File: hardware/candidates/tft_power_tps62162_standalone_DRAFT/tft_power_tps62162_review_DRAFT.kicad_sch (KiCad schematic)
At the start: 8 parts, among them U301 TPS62162DSGR

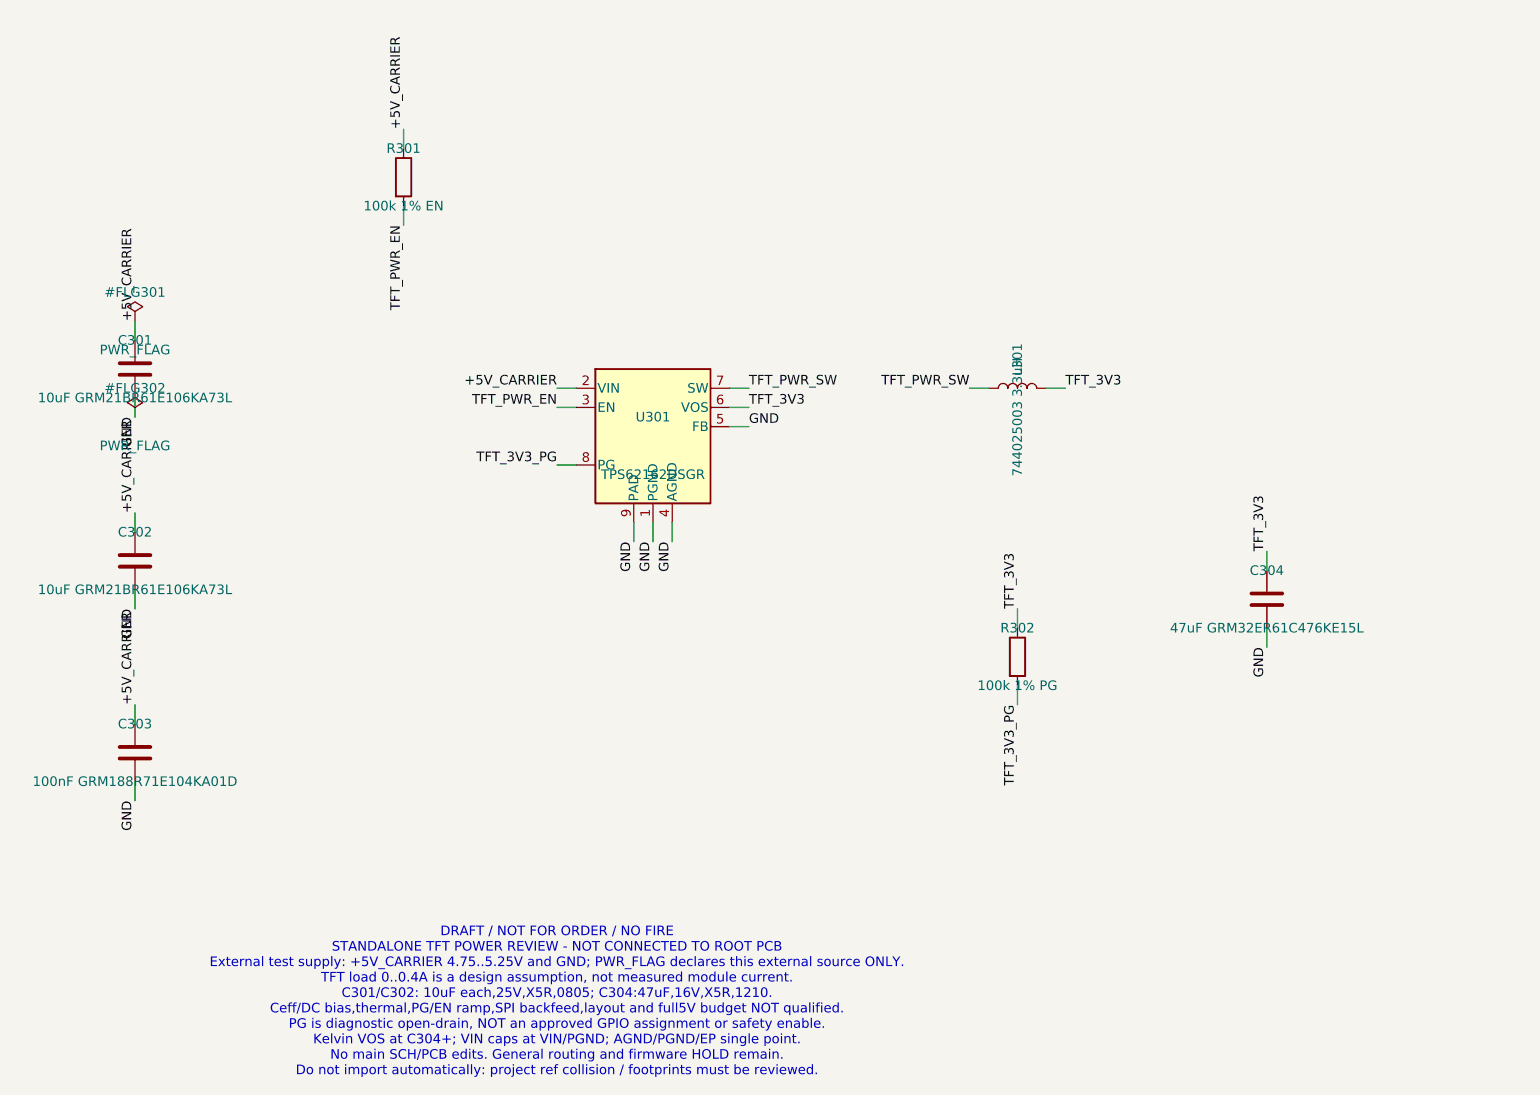
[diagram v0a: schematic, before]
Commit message: hardware: fix TPS62162 draft fields and identify pull-ups
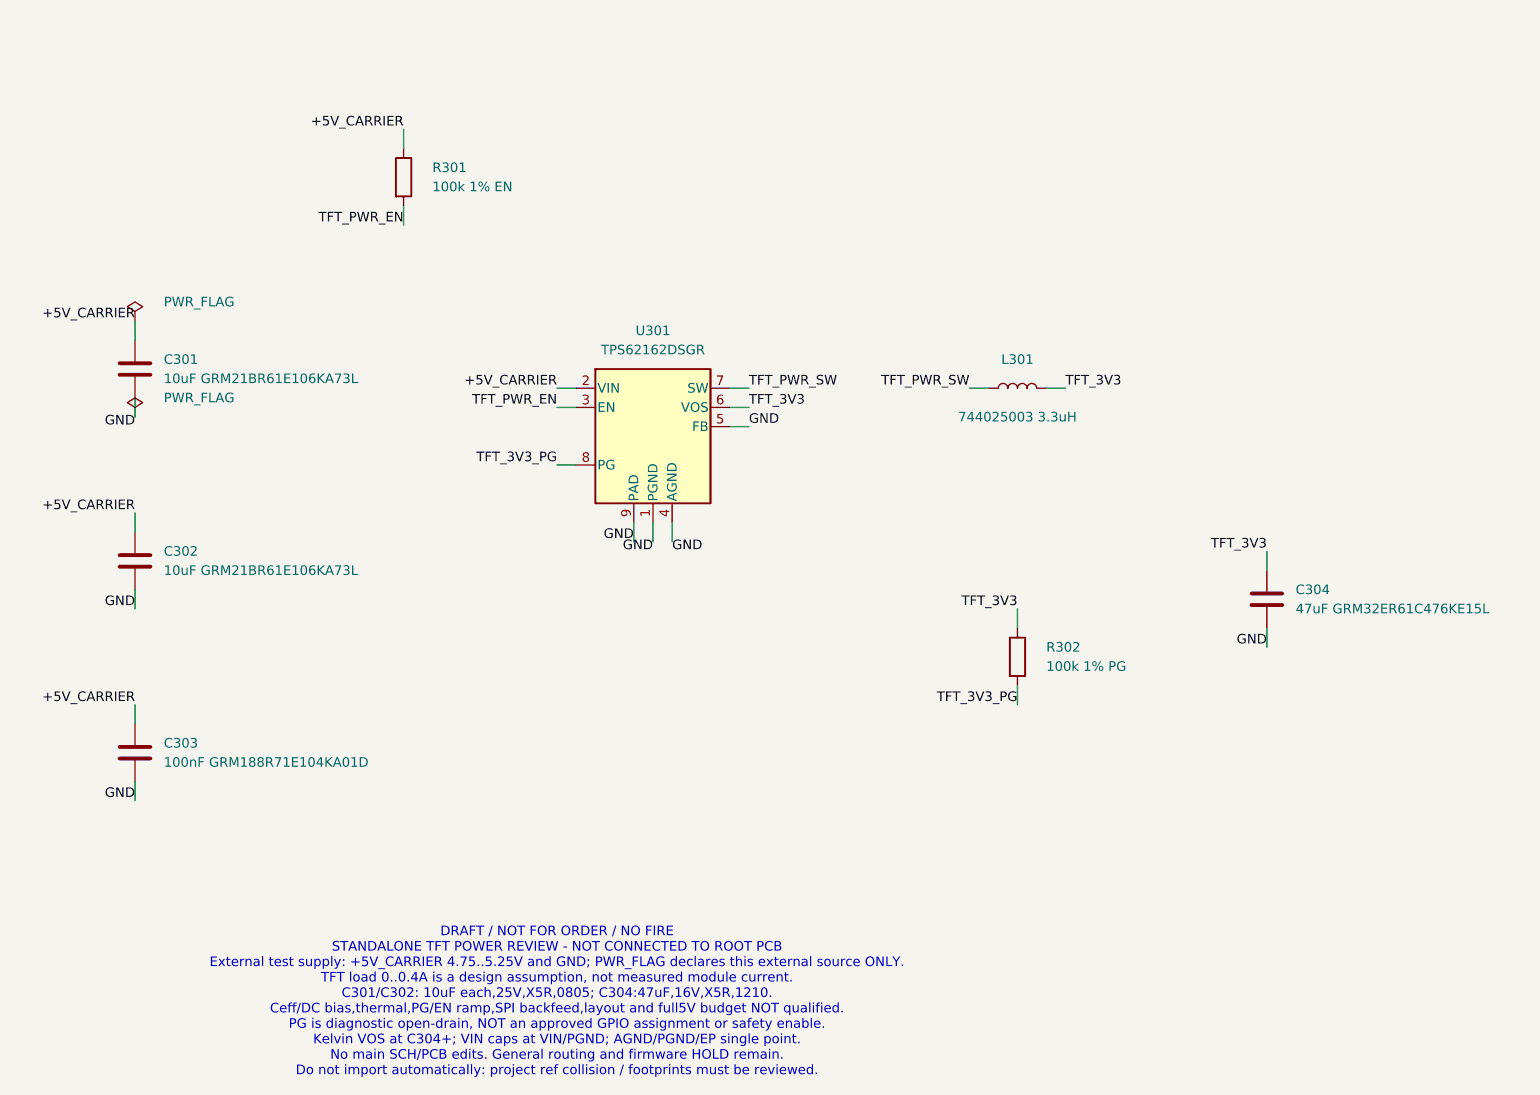
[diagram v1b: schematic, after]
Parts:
- R301, R302: MPN (none) -> RC0603FR-07100KL; Manufacturer (none) -> Yageo; Supplier (none) -> ChipDip9000632023; Supplier_URL (none) -> https://www.chipdip.ru/product/rc0603fr-07100kl
